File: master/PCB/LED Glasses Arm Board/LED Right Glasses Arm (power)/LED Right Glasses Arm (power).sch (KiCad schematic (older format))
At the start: 12 parts, among them U1 TPS63060

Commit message: power reg circuit
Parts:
- removed C: 10uF, symbol Device:C_Small
- removed C? (x2): 22uF, symbol Device:C_Small
- added D? (x2): LED, symbol Device:LED
- added R? (x2): 2k2, symbol Device:R_Small_US
- added SW?: SW_SPST, symbol Switch:SW_SPST
- C: value 10uF -> 20u
- C: value 0.1uF -> 0.1u
- C?: value 10pF -> 10p
- C?: value 22uF -> 66u
- L?: value 1uH -> 1u
- R?: value 1MOhm -> 1M
- R?: value 111kOhm -> 111k
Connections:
- wire segments 37 -> 38
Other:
- moved on the sheet: C
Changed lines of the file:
@@
 VIN
-Wire Wire Line
-	2300 5000 2150 5000
-Wire Wire Line
-	2150 5000 2150 4900
-Connection ~ 2150 4900
-Wire Wire Line
-	2150 4900 2300 4900
 Wire Wire Line
 	2300 5300 2150 5300
@@
 L power:GND #PWR?
 U 1 1 5F4B6F97
-P 950 5700
-F 0 "#PWR?" H 950 5450 50  0001 C CNN
-F 1 "GND" H 955 5527 50  0000 C CNN
-F 2 "" H 950 5700 50  0001 C CNN
-F 3 "" H 950 5700 50  0001 C CNN
-	1    950  5700
+P 1200 5700
+F 0 "#PWR?" H 1200 5450 50  0001 C CNN
+F 1 "GND" H 1205 5527 50  0000 C CNN
+F 2 "" H 1200 5700 50  0001 C CNN
+F 3 "" H 1200 5700 50  0001 C CNN
+	1    1200 5700
 	1    0    0    -1
 $EndComp
@@
 $Comp
 L Device:C_Small C
-U 1 1 5F4B7066
-P 800 5300
-F 0 "C" H 892 5346 50  0000 L CNN
-F 1 "10uF" H 892 5255 50  0000 L CNN
-F 2 "" H 800 5300 50  0001 C CNN
-F 3 "~" H 800 5300 50  0001 C CNN
-	1    800  5300
-	1    0    0    -1
-$EndComp
-$Comp
-L Device:C_Small C
 U 1 1 5F4B72C8
-P 1100 5300
-F 0 "C" H 1192 5346 50  0000 L CNN
-F 1 "10uF" H 1192 5255 50  0000 L CNN
-F 2 "" H 1100 5300 50  0001 C CNN
-F 3 "~" H 1100 5300 50  0001 C CNN
-	1    1100 5300
-	1    0    0    -1
-$EndComp
-Wire Wire Line
-	800  5400 950  5400
-Wire Wire Line
-	800  5200 950  5200
-Wire Wire Line
-	600  4900 950  4900
-Wire Wire Line
-	950  5200 950  4900
-Connection ~ 950  5200
-Wire Wire Line
-	950  5200 1100 5200
-Connection ~ 950  4900
-Wire Wire Line
-	950  4900 2150 4900
-Wire Wire Line
-	950  5400 950  5700
-Connection ~ 950  5400
-Wire Wire Line
-	950  5400 1100 5400
+P 1200 5300
+F 0 "C" H 1292 5346 50  0000 L CNN
+F 1 "20u" H 1292 5255 50  0000 L CNN
+F 2 "" H 1200 5300 50  0001 C CNN
+F 3 "~" H 1200 5300 50  0001 C CNN
+	1    1200 5300
+	1    0    0    -1
+$EndComp
+Wire Wire Line
+	1200 5200 1200 4900
+Wire Wire Line
+	1200 5400 1200 5700
 $Comp
 L Device:C_Small C
@@
 P 1750 5400
 F 0 "C" H 1842 5446 50  0000 L CNN
-F 1 "0.1uF" H 1842 5355 50  0000 L CNN
+F 1 "0.1u" H 1842 5355 50  0000 L CNN
 F 2 "" H 1750 5400 50  0001 C CNN
 F 3 "~" H 1750 5400 50  0001 C CNN
@@
 P 2700 4150
 F 0 "L?" H 2700 4365 50  0000 C CNN
-F 1 "1uH" H 2700 4274 50  0000 C CNN
+F 1 "1u" H 2700 4274 50  0000 C CNN
 F 2 "" H 2700 4150 50  0001 C CNN
 F 3 "~" H 2700 4150 50  0001 C CNN
@@
 P 3200 5000
 F 0 "R?" H 3268 5046 50  0000 L CNN
-F 1 "1MOhm" H 3268 4955 50  0000 L CNN
+F 1 "1M" H 3268 4955 50  0000 L CNN
 F 2 "" H 3200 5000 50  0001 C CNN
 F 3 "~" H 3200 5000 50  0001 C CNN
@@
 P 3200 5200
 F 0 "R?" H 3268 5246 50  0000 L CNN
-F 1 "111kOhm" H 3268 5155 50  0000 L CNN
+F 1 "111k" H 3268 5155 50  0000 L CNN
 F 2 "" H 3200 5200 50  0001 C CNN
 F 3 "~" H 3200 5200 50  0001 C CNN
@@
 P 3900 5200
 F 0 "C?" H 3992 5246 50  0000 L CNN
-F 1 "10pF" H 3992 5155 50  0000 L CNN
+F 1 "10p" H 3992 5155 50  0000 L CNN
 F 2 "" H 3900 5200 50  0001 C CNN
 F 3 "~" H 3900 5200 50  0001 C CNN
@@
 $Comp
 L Device:C_Small C?
-U 1 1 5F4BC93C
-P 4750 5300
-F 0 "C?" H 4842 5346 50  0000 L CNN
-F 1 "22uF" H 4842 5255 50  0000 L CNN
-F 2 "" H 4750 5300 50  0001 C CNN
-F 3 "~" H 4750 5300 50  0001 C CNN
-	1    4750 5300
-	1    0    0    -1
-$EndComp
-$Comp
-L Device:C_Small C?
 U 1 1 5F4BC943
 P 5050 5300
 F 0 "C?" H 5142 5346 50  0000 L CNN
-F 1 "22uF" H 5142 5255 50  0000 L CNN
+F 1 "66u" H 5142 5255 50  0000 L CNN
 F 2 "" H 5050 5300 50  0001 C CNN
 F 3 "~" H 5050 5300 50  0001 C CNN
@@
 	1    0    0    -1
 $EndComp
-$Comp
-L Device:C_Small C?
-U 1 1 5F4BCD98
-P 5450 5300
-F 0 "C?" H 5542 5346 50  0000 L CNN
-F 1 "22uF" H 5542 5255 50  0000 L CNN
-F 2 "" H 5450 5300 50  0001 C CNN
-F 3 "~" H 5450 5300 50  0001 C CNN
-	1    5450 5300
-	1    0    0    -1
-$EndComp
-Wire Wire Line
-	4750 5200 5050 5200
-Wire Wire Line
-	4750 5400 5050 5400
-Wire Wire Line
-	5050 5200 5450 5200
-Connection ~ 5050 5200
-Wire Wire Line
-	5050 5400 5450 5400
-Connection ~ 5050 5400
 Wire Wire Line
 	5050 5200 5050 4900
@@
 Wire Wire Line
 	5050 5400 5050 5550
-Wire Wire Line
-	5050 4900 5450 4900
-Connection ~ 5050 4900
-Text Label 5300 4900 0    50   ~ 0
+Text Label 6500 4900 0    50   ~ 0
 VOUT
-Wire Wire Line
-	4300 5650 4300 5850
 Connection ~ 4300 5650
 Text Label 4300 5850 0    50   ~ 0
 PG
+Connection ~ 1200 4900
+Wire Wire Line
+	600  4900 800  4900
+Wire Wire Line
+	1200 4900 2300 4900
+Wire Wire Line
+	2300 5000 1650 5000
+Wire Wire Line
+	1650 5000 1650 6250
+Wire Wire Line
+	800  6250 800  4900
+Connection ~ 800  4900
+Wire Wire Line
+	800  4900 1200 4900
+$Comp
+L Switch:SW_SPST SW?
+U 1 1 5F4C134D
+P 1300 6250
+F 0 "SW?" H 1300 6485 50  0000 C CNN
+F 1 "SW_SPST" H 1300 6394 50  0000 C CNN
+F 2 "" H 1300 6250 50  0001 C CNN
+F 3 "" H 1300 6250 50  0001 C CNN
+	1    1300 6250
+	1    0    0    -1
+$EndComp
+Wire Wire Line
+	800  6250 1100 6250
+Wire Wire Line
+	1500 6250 1650 6250
+$Comp
+L Device:LED D?
+U 1 1 5F4C82CF
+P 6000 5450
+F 0 "D?" H 5992 5666 50  0000 C CNN
+F 1 "LED" H 5992 5575 50  0000 C CNN
+F 2 "" H 6000 5450 50  0001 C CNN
+F 3 "~" H 6000 5450 50  0001 C CNN
+	1    6000 5450
+	0    1    -1   0
+$EndComp
+$Comp
+L Device:R_Small_US R?
+U 1 1 5F4C82D6
+P 6000 5900
+F 0 "R?" H 6068 5946 50  0000 L CNN
+F 1 "2k2" H 6068 5855 50  0000 L CNN
+F 2 "" H 6000 5900 50  0001 C CNN
+F 3 "~" H 6000 5900 50  0001 C CNN
+	1    6000 5900
+	1    0    0    -1
+$EndComp
+Wire Wire Line
+	6000 5600 6000 5800
+Wire Wire Line
+	6000 6000 6000 6500
+Wire Wire Line
+	5050 4900 6000 4900
+Connection ~ 5050 4900
+Wire Wire Line
+	6000 4900 6000 5300
+Connection ~ 6000 4900
+Wire Wire Line
+	6000 4900 6650 4900
+$Comp
+L power:GND #PWR?
+U 1 1 5F4CC68F
+P 6000 6500
+F 0 "#PWR?" H 6000 6250 50  0001 C CNN
+F 1 "GND" H 6005 6327 50  0000 C CNN
+F 2 "" H 6000 6500 50  0001 C CNN
+F 3 "" H 6000 6500 50  0001 C CNN
+	1    6000 6500
+	1    0    0    -1
+$EndComp
+$Comp
+L Device:LED D?
+U 1 1 5F4CC9A9
+P 1800 6250
+F 0 "D?" H 1792 6466 50  0000 C CNN
+F 1 "LED" H 1792 6375 50  0000 C CNN
+F 2 "" H 1800 6250 50  0001 C CNN
+F 3 "~" H 1800 6250 50  0001 C CNN
+	1    1800 6250
+	-1   0    0    -1
+$EndComp
+$Comp
+L Device:R_Small_US R?
+U 1 1 5F4CC9B0
+P 2250 6250
+F 0 "R?" V 2455 6250 50  0000 C CNN
+F 1 "2k2" V 2364 6250 50  0000 C CNN
+F 2 "" H 2250 6250 50  0001 C CNN
+F 3 "~" H 2250 6250 50  0001 C CNN
+	1    2250 6250
+	0    -1   -1   0
+$EndComp
+Wire Wire Line
+	1950 6250 2150 6250
+Connection ~ 1650 6250
+Wire Wire Line
+	4300 5650 4300 6250
+Wire Wire Line
+	2350 6250 4300 6250
 $EndSCHEMATC

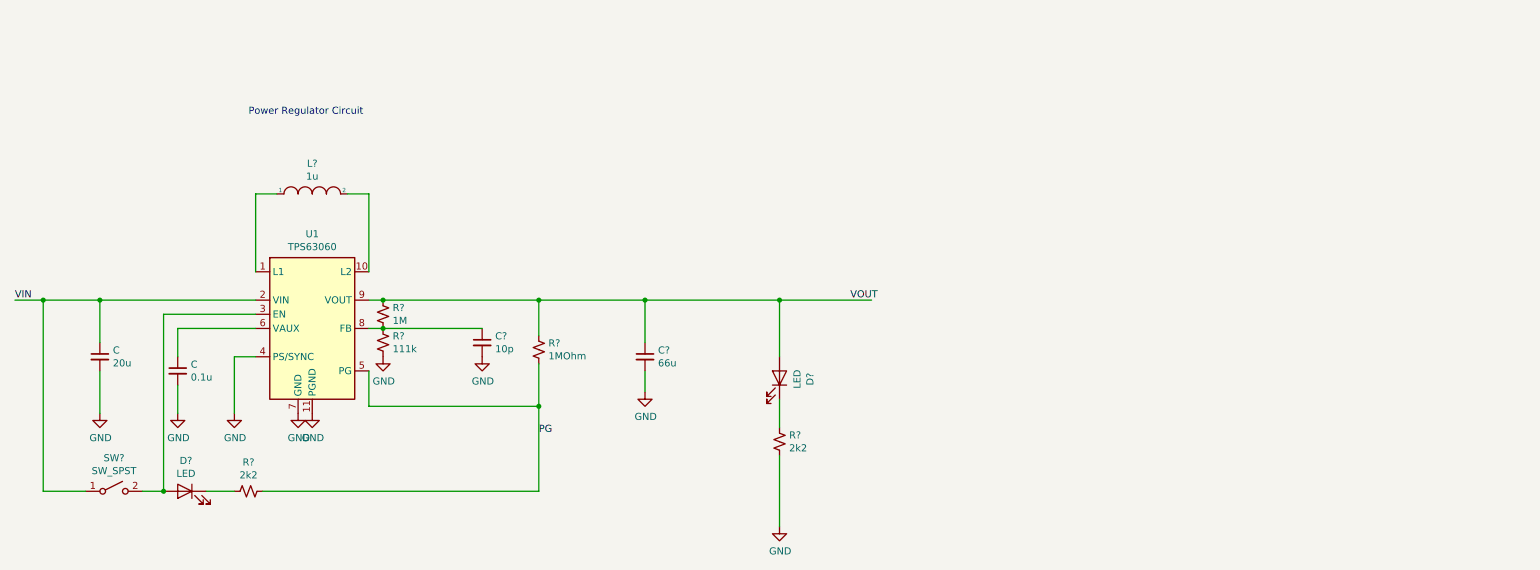
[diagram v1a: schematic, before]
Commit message: updated
added polarity protection
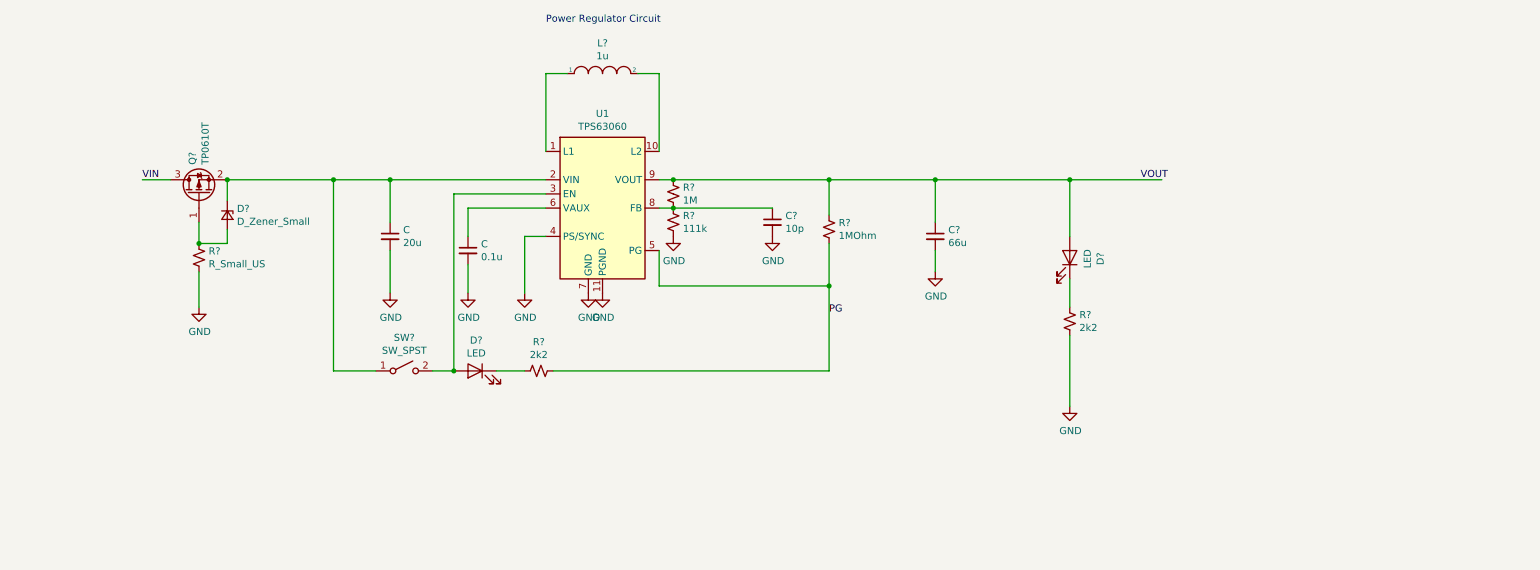
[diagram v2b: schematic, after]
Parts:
- added D?: D_Zener_Small, symbol Device:D_Zener_Small
- added Q?: TP0610T, Package_TO_SOT_SMD:SOT-23, symbol Transistor_FET:TP0610T
- added R?: R_Small_US, symbol Device:R_Small_US
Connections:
- net GND: now also R?.2
- net VIN: now also Q?.3 (D); no longer C.1, SW?.1 (A), U1.2 (VIN)
- new net: C.1, D?.1 (K), Q?.2 (S), SW?.1 (A), U1.2 (VIN)
- new net: D?.2 (A), Q?.1 (G), R?.1
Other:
- moved on the sheet: C, C?, D?, L?, R?, SW?, U1

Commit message: Started on the PCB
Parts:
- C1, C2: renamed from C; footprint (none) -> Capacitor_SMD:C_0603_1608Metric
- C3, C4: renamed from C?; footprint (none) -> Capacitor_SMD:C_0603_1608Metric
- D1: renamed from D?; footprint (none) -> Diode_SMD:D_0603_1608Metric
- D2, D3: renamed from D?; footprint (none) -> LED_SMD:LED_0603_1608Metric
- L1: renamed from L?; footprint (none) -> Inductor_SMD:L_Coilcraft_XxL4020
- R1, R2, R3, R4, R5, R6: renamed from R?; footprint (none) -> Resistor_SMD:R_0603_1608Metric
- SW1: renamed from SW?; footprint (none) -> Button_Switch_SMD:SW_SPST_FSMSM
- gave numbers to parts that had none: 1
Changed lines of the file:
@@
 	4350 4250 3800 4250
 $Comp
-L power:GND #PWR?
+L power:GND #PWR0101
 U 1 1 5F4B6F4F
 P 4200 4850
-F 0 "#PWR?" H 4200 4600 50  0001 C CNN
+F 0 "#PWR0101" H 4200 4600 50  0001 C CNN
 F 1 "GND" H 4205 4677 50  0000 C CNN
 F 2 "" H 4200 4850 50  0001 C CNN
@@
 $EndComp
 $Comp
-L power:GND #PWR?
+L power:GND #PWR0102
 U 1 1 5F4B6F73
 P 3800 4850
-F 0 "#PWR?" H 3800 4600 50  0001 C CNN
+F 0 "#PWR0102" H 3800 4600 50  0001 C CNN
 F 1 "GND" H 3805 4677 50  0000 C CNN
 F 2 "" H 3800 4850 50  0001 C CNN
@@
 $EndComp
 $Comp
-L power:GND #PWR?
+L power:GND #PWR0103
 U 1 1 5F4B6F97
 P 3250 4850
-F 0 "#PWR?" H 3250 4600 50  0001 C CNN
+F 0 "#PWR0103" H 3250 4600 50  0001 C CNN
 F 1 "GND" H 3255 4677 50  0000 C CNN
 F 2 "" H 3250 4850 50  0001 C CNN
@@
 $EndComp
 $Comp
-L power:GND #PWR?
+L power:GND #PWR0104
 U 1 1 5F4B6FC9
 P 4650 4850
-F 0 "#PWR?" H 4650 4600 50  0001 C CNN
+F 0 "#PWR0104" H 4650 4600 50  0001 C CNN
 F 1 "GND" H 4655 4677 50  0000 C CNN
 F 2 "" H 4650 4850 50  0001 C CNN
@@
 $EndComp
 $Comp
-L power:GND #PWR?
+L power:GND #PWR0105
 U 1 1 5F4B6FED
 P 4750 4850
-F 0 "#PWR?" H 4750 4600 50  0001 C CNN
+F 0 "#PWR0105" H 4750 4600 50  0001 C CNN
 F 1 "GND" H 4755 4677 50  0000 C CNN
 F 2 "" H 4750 4850 50  0001 C CNN
@@
 $EndComp
 $Comp
-L Device:C_Small C
+L Device:C_Small C1
 U 1 1 5F4B72C8
 P 3250 4450
-F 0 "C" H 3342 4496 50  0000 L CNN
+F 0 "C1" H 3342 4496 50  0000 L CNN
 F 1 "20u" H 3342 4405 50  0000 L CNN
-F 2 "" H 3250 4450 50  0001 C CNN
+F 2 "Capacitor_SMD:C_0603_1608Metric" H 3250 4450 50  0001 C CNN
 F 3 "~" H 3250 4450 50  0001 C CNN
 	1    3250 4450
@@
 	3250 4550 3250 4850
 $Comp
-L Device:C_Small C
+L Device:C_Small C2
 U 1 1 5F4B8E20
 P 3800 4550
-F 0 "C" H 3892 4596 50  0000 L CNN
+F 0 "C2" H 3892 4596 50  0000 L CNN
 F 1 "0.1u" H 3892 4505 50  0000 L CNN
-F 2 "" H 3800 4550 50  0001 C CNN
+F 2 "Capacitor_SMD:C_0603_1608Metric" H 3800 4550 50  0001 C CNN
 F 3 "~" H 3800 4550 50  0001 C CNN
 	1    3800 4550
@@
 $EndComp
 $Comp
-L pspice:INDUCTOR L?
+L pspice:INDUCTOR L1
 U 1 1 5F4B9710
 P 4750 3300
-F 0 "L?" H 4750 3515 50  0000 C CNN
+F 0 "L1" H 4750 3515 50  0000 C CNN
 F 1 "1u" H 4750 3424 50  0000 C CNN
-F 2 "" H 4750 3300 50  0001 C CNN
+F 2 "Inductor_SMD:L_Coilcraft_XxL4020" H 4750 3300 50  0001 C CNN
 F 3 "~" H 4750 3300 50  0001 C CNN
 	1    4750 3300
@@
 	5150 4050 5250 4050
 $Comp
-L Device:R_Small_US R?
+L Device:R_Small_US R3
 U 1 1 5F4BA20C
 P 5250 4150
-F 0 "R?" H 5318 4196 50  0000 L CNN
+F 0 "R3" H 5318 4196 50  0000 L CNN
 F 1 "1M" H 5318 4105 50  0000 L CNN
-F 2 "" H 5250 4150 50  0001 C CNN
+F 2 "Resistor_SMD:R_0603_1608Metric" H 5250 4150 50  0001 C CNN
 F 3 "~" H 5250 4150 50  0001 C CNN
 	1    5250 4150
@@
 	5150 4250 5250 4250
 $Comp
-L Device:R_Small_US R?
+L Device:R_Small_US R4
 U 1 1 5F4BA598
 P 5250 4350
-F 0 "R?" H 5318 4396 50  0000 L CNN
+F 0 "R4" H 5318 4396 50  0000 L CNN
 F 1 "111k" H 5318 4305 50  0000 L CNN
-F 2 "" H 5250 4350 50  0001 C CNN
+F 2 "Resistor_SMD:R_0603_1608Metric" H 5250 4350 50  0001 C CNN
 F 3 "~" H 5250 4350 50  0001 C CNN
 	1    5250 4350
@@
 	5150 4550 5150 4800
 $Comp
-L power:GND #PWR?
+L power:GND #PWR0106
 U 1 1 5F4BAEF0
 P 5250 4450
-F 0 "#PWR?" H 5250 4200 50  0001 C CNN
+F 0 "#PWR0106" H 5250 4200 50  0001 C CNN
 F 1 "GND" H 5255 4277 50  0000 C CNN
 F 2 "" H 5250 4450 50  0001 C CNN
@@
 Connection ~ 5250 4250
 $Comp
-L Device:C_Small C?
+L Device:C_Small C3
 U 1 1 5F4BB248
 P 5950 4350
-F 0 "C?" H 6042 4396 50  0000 L CNN
+F 0 "C3" H 6042 4396 50  0000 L CNN
 F 1 "10p" H 6042 4305 50  0000 L CNN
-F 2 "" H 5950 4350 50  0001 C CNN
+F 2 "Capacitor_SMD:C_0603_1608Metric" H 5950 4350 50  0001 C CNN
 F 3 "~" H 5950 4350 50  0001 C CNN
 	1    5950 4350
@@
 	5250 4250 5950 4250
 $Comp
-L power:GND #PWR?
+L power:GND #PWR0107
 U 1 1 5F4BBACE
 P 5950 4450
-F 0 "#PWR?" H 5950 4200 50  0001 C CNN
+F 0 "#PWR0107" H 5950 4200 50  0001 C CNN
 F 1 "GND" H 5955 4277 50  0000 C CNN
 F 2 "" H 5950 4450 50  0001 C CNN
@@
 $EndComp
 $Comp
-L Device:R_Small_US R?
+L Device:R_Small_US R5
 U 1 1 5F4BBDC6
 P 6350 4400
-F 0 "R?" H 6418 4446 50  0000 L CNN
+F 0 "R5" H 6418 4446 50  0000 L CNN
 F 1 "1MOhm" H 6418 4355 50  0000 L CNN
-F 2 "" H 6350 4400 50  0001 C CNN
+F 2 "Resistor_SMD:R_0603_1608Metric" H 6350 4400 50  0001 C CNN
 F 3 "~" H 6350 4400 50  0001 C CNN
 	1    6350 4400
@@
 Connection ~ 6350 4050
 $Comp
-L Device:C_Small C?
+L Device:C_Small C4
 U 1 1 5F4BC943
 P 7100 4450
-F 0 "C?" H 7192 4496 50  0000 L CNN
+F 0 "C4" H 7192 4496 50  0000 L CNN
 F 1 "66u" H 7192 4405 50  0000 L CNN
-F 2 "" H 7100 4450 50  0001 C CNN
+F 2 "Capacitor_SMD:C_0603_1608Metric" H 7100 4450 50  0001 C CNN
 F 3 "~" H 7100 4450 50  0001 C CNN
 	1    7100 4450
@@
 	6350 4050 7100 4050
 $Comp
-L power:GND #PWR?
+L power:GND #PWR0108
 U 1 1 5F4BEA89
 P 7100 4700
-F 0 "#PWR?" H 7100 4450 50  0001 C CNN
+F 0 "#PWR0108" H 7100 4450 50  0001 C CNN
 F 1 "GND" H 7105 4527 50  0000 C CNN
 F 2 "" H 7100 4700 50  0001 C CNN
@@
 	2850 4050 3250 4050
 $Comp
-L Switch:SW_SPST SW?
+L Switch:SW_SPST SW1
 U 1 1 5F4C134D
 P 3350 5400
-F 0 "SW?" H 3350 5635 50  0000 C CNN
+F 0 "SW1" H 3350 5635 50  0000 C CNN
 F 1 "SW_SPST" H 3350 5544 50  0000 C CNN
-F 2 "" H 3350 5400 50  0001 C CNN
+F 2 "Button_Switch_SMD:SW_SPST_FSMSM" H 3350 5400 50  0001 C CNN
 F 3 "" H 3350 5400 50  0001 C CNN
 	1    3350 5400
@@
 	3550 5400 3700 5400
 $Comp
-L Device:LED D?
+L Device:LED D3
 U 1 1 5F4C82CF
 P 8050 4600
-F 0 "D?" H 8042 4816 50  0000 C CNN
+F 0 "D3" H 8042 4816 50  0000 C CNN
 F 1 "LED" H 8042 4725 50  0000 C CNN
-F 2 "" H 8050 4600 50  0001 C CNN
+F 2 "LED_SMD:LED_0603_1608Metric" H 8050 4600 50  0001 C CNN
 F 3 "~" H 8050 4600 50  0001 C CNN
 	1    8050 4600
@@
 $EndComp
 $Comp
-L Device:R_Small_US R?
+L Device:R_Small_US R6
 U 1 1 5F4C82D6
 P 8050 5050
-F 0 "R?" H 8118 5096 50  0000 L CNN
+F 0 "R6" H 8118 5096 50  0000 L CNN
 F 1 "2k2" H 8118 5005 50  0000 L CNN
-F 2 "" H 8050 5050 50  0001 C CNN
+F 2 "Resistor_SMD:R_0603_1608Metric" H 8050 5050 50  0001 C CNN
 F 3 "~" H 8050 5050 50  0001 C CNN
 	1    8050 5050
@@
 	8050 4050 8700 4050
 $Comp
-L power:GND #PWR?
+L power:GND #PWR0109
 U 1 1 5F4CC68F
 P 8050 5650
-F 0 "#PWR?" H 8050 5400 50  0001 C CNN
+F 0 "#PWR0109" H 8050 5400 50  0001 C CNN
 F 1 "GND" H 8055 5477 50  0000 C CNN
 F 2 "" H 8050 5650 50  0001 C CNN
@@
 $EndComp
 $Comp
-L Device:LED D?
+L Device:LED D2
 U 1 1 5F4CC9A9
 P 3850 5400
-F 0 "D?" H 3842 5616 50  0000 C CNN
+F 0 "D2" H 3842 5616 50  0000 C CNN
 F 1 "LED" H 3842 5525 50  0000 C CNN
-F 2 "" H 3850 5400 50  0001 C CNN
+F 2 "LED_SMD:LED_0603_1608Metric" H 3850 5400 50  0001 C CNN
 F 3 "~" H 3850 5400 50  0001 C CNN
 	1    3850 5400
@@
 $EndComp
 $Comp
-L Device:R_Small_US R?
+L Device:R_Small_US R2
 U 1 1 5F4CC9B0
 P 4300 5400
-F 0 "R?" V 4505 5400 50  0000 C CNN
+F 0 "R2" V 4505 5400 50  0000 C CNN
 F 1 "2k2" V 4414 5400 50  0000 C CNN
-F 2 "" H 4300 5400 50  0001 C CNN
+F 2 "Resistor_SMD:R_0603_1608Metric" H 4300 5400 50  0001 C CNN
 F 3 "~" H 4300 5400 50  0001 C CNN
 	1    4300 5400
@@
 	1500 4050 1700 4050
 $Comp
-L Device:D_Zener_Small D?
+L Device:D_Zener_Small D1
 U 1 1 5F7F1725
 P 2100 4300
-F 0 "D?" V 2054 4368 50  0000 L CNN
+F 0 "D1" V 2054 4368 50  0000 L CNN
 F 1 "D_Zener_Small" V 2145 4368 50  0000 L CNN
-F 2 "" V 2100 4300 50  0001 C CNN
+F 2 "Diode_SMD:D_0603_1608Metric" V 2100 4300 50  0001 C CNN
 F 3 "~" V 2100 4300 50  0001 C CNN
 	1    2100 4300
@@
 $EndComp
 $Comp
-L Device:R_Small_US R?
+L Device:R_Small_US R1
 U 1 1 5F7F24DD
 P 1900 4600
-F 0 "R?" H 1968 4646 50  0000 L CNN
+F 0 "R1" H 1968 4646 50  0000 L CNN
 F 1 "R_Small_US" H 1968 4555 50  0000 L CNN
-F 2 "" H 1900 4600 50  0001 C CNN
+F 2 "Resistor_SMD:R_0603_1608Metric" H 1900 4600 50  0001 C CNN
 F 3 "~" H 1900 4600 50  0001 C CNN
 	1    1900 4600
@@
 $EndComp
 $Comp
-L power:GND #PWR?
+L power:GND #PWR0110
 U 1 1 5F7F25B0
 P 1900 4950
-F 0 "#PWR?" H 1900 4700 50  0001 C CNN
+F 0 "#PWR0110" H 1900 4700 50  0001 C CNN
 F 1 "GND" H 1905 4777 50  0000 C CNN
 F 2 "" H 1900 4950 50  0001 C CNN
@@
 	2100 4500 2100 4400
 $Comp
-L Transistor_FET:TP0610T Q?
+L Transistor_FET:TP0610T Q1
 U 1 1 5F7F3597
 P 1900 4150
-F 0 "Q?" H 2106 4196 50  0000 L CNN
+F 0 "Q1" H 2106 4196 50  0000 L CNN
 F 1 "TP0610T" H 2106 4105 50  0000 L CNN
 F 2 "Package_TO_SOT_SMD:SOT-23" H 2100 4075 50  0001 L CIN
